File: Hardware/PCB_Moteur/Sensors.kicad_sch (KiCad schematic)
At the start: 18 parts, among them J18 Screw_Terminal_01x04, J3 Screw_Terminal_01x04, U8 INA125UA/2K5, U9 MAX6612MXK

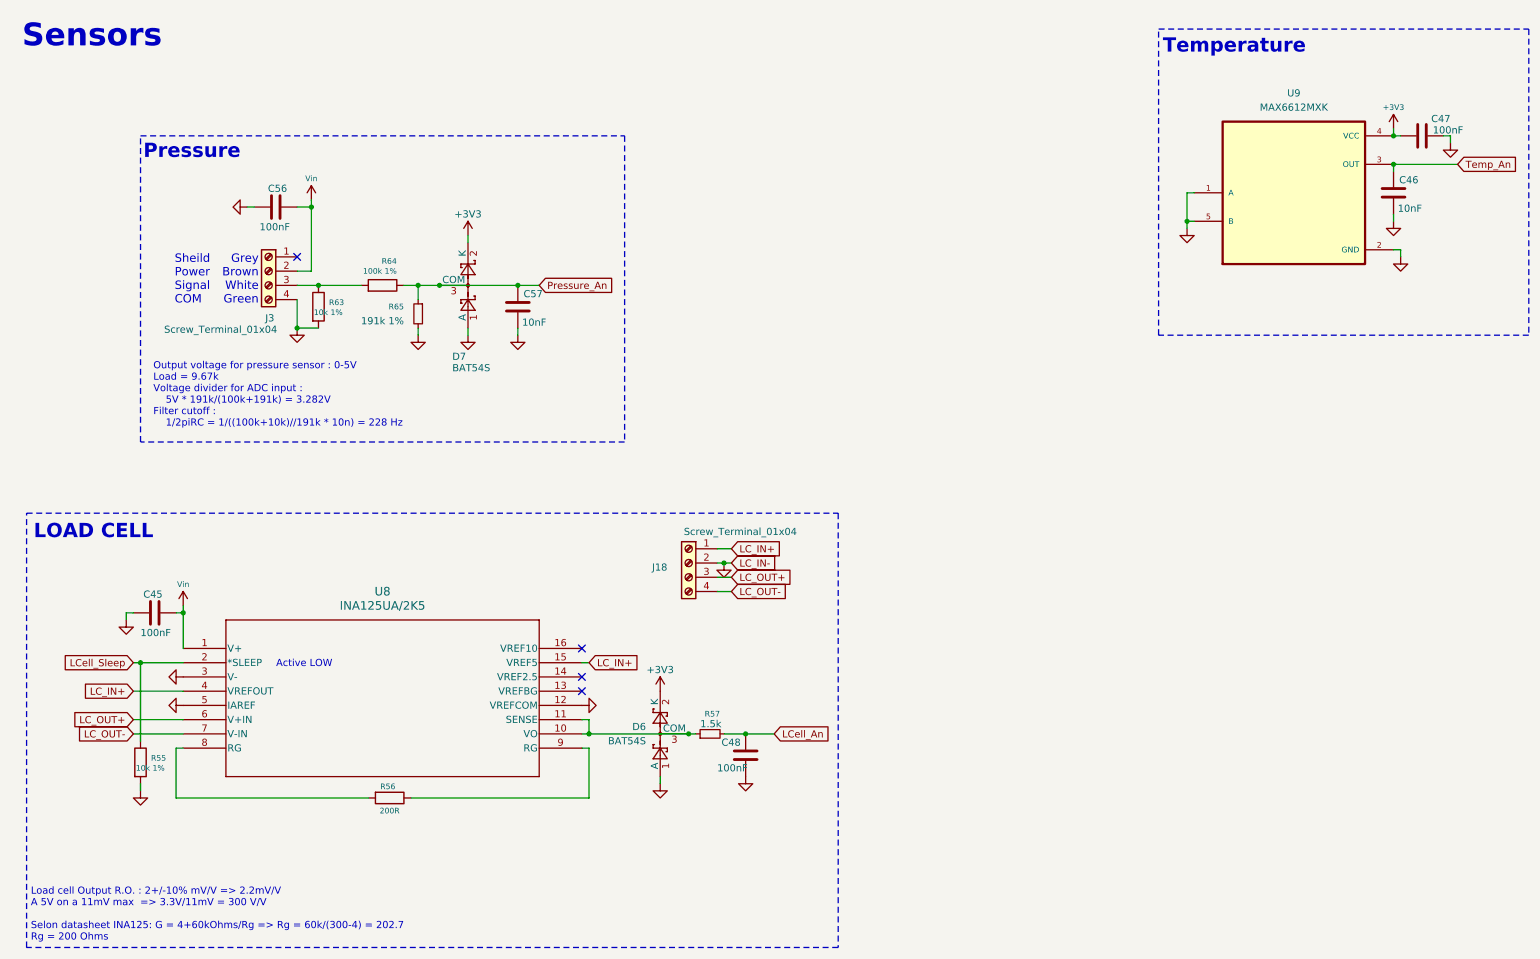
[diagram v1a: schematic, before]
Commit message: wip : reorder refdes and fix footprints
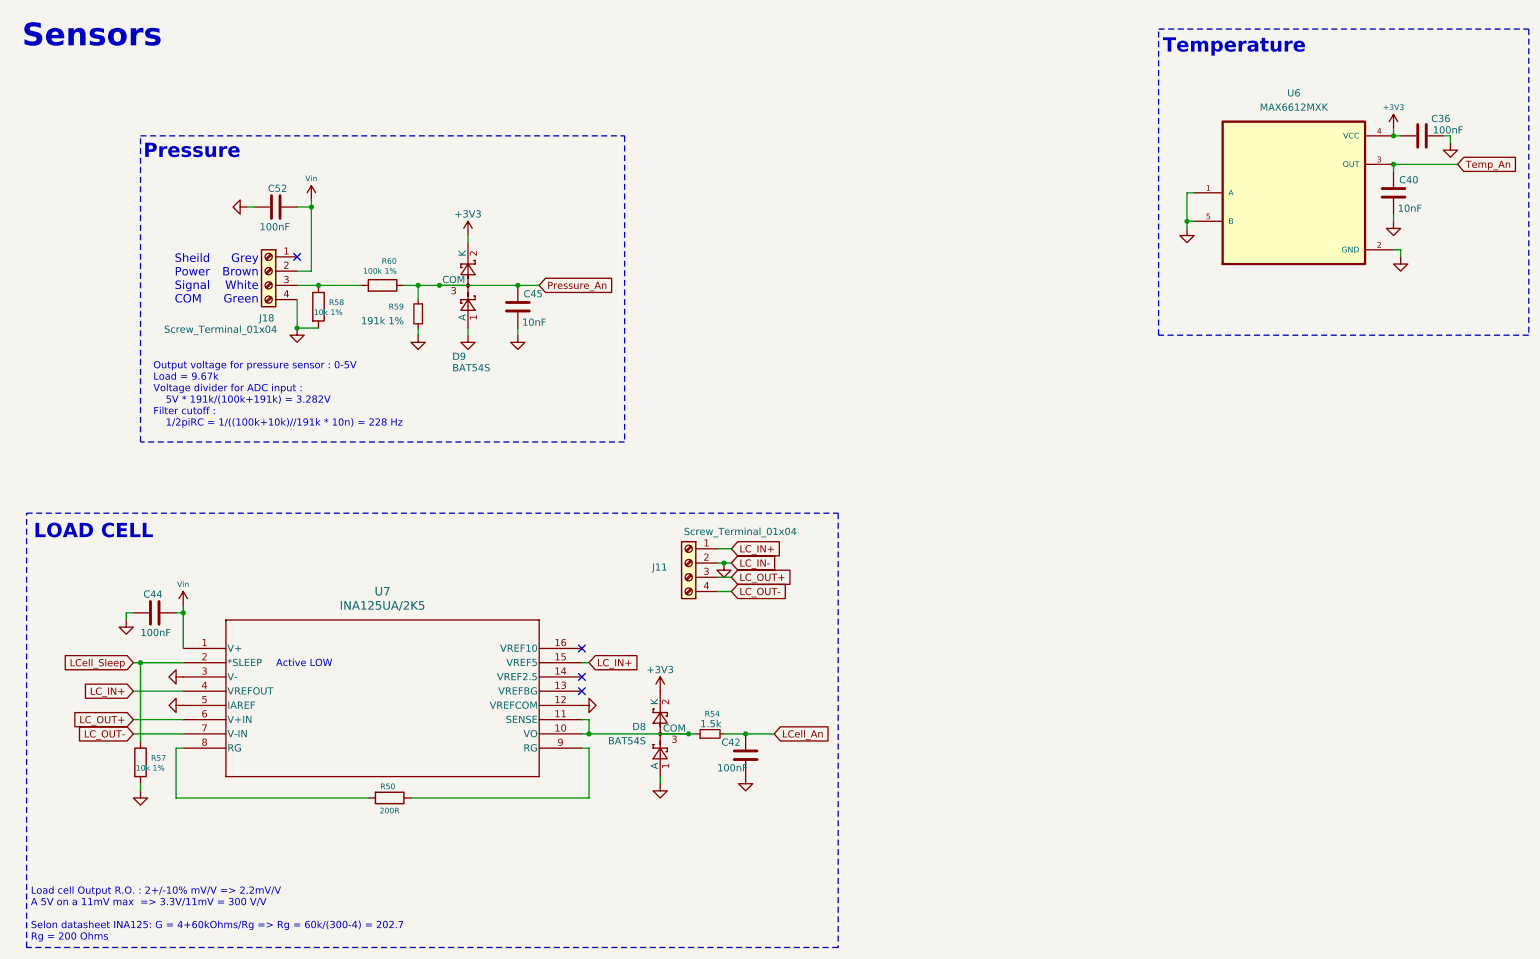
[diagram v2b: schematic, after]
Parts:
- U7: renamed from U8; DigiKey_Part_Number  (none) -> 296-50343-1-ND
- renumbered C47 to C36, C46 to C40, C48 to C42, C45 to C44, C57 to C45, C56 to C52, D6 to D8, D7 to D9, J18 to J11, J3 to J18, R56 to R50, R57 to R54, R55 to R57, R63 to R58, R65 to R59, R64 to R60, U9 to U6
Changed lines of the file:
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@@
 		(dnp no)
 		(fields_autoplaced yes)
-		(property "Reference" "D6"
+		(property "Reference" "D8"
 			(at 124.46 139.6999 90)
 			(effects
@@
 			(project "PCB_moteur"
 				(path "/b0d87684-7b1c-41d8-8358-755aa327573e/f31687d3-ca84-4d71-914a-32b6c2b363a9"
-					(reference "D6")
+					(reference "D8")
 					(unit 1)
 				)
@@
 		(on_board yes)
 		(dnp no)
-		(property "Reference" "R57"
+		(property "Reference" "R54"
 			(at 137.668 137.414 90)
 			(effects
@@
 			(project "PCB_moteur"
 				(path "/b0d87684-7b1c-41d8-8358-755aa327573e/f31687d3-ca84-4d71-914a-32b6c2b363a9"
-					(reference "R57")
+					(reference "R54")
 					(unit 1)
 				)
@@
 		(on_board yes)
 		(dnp no)
-		(property "Reference" "C47"
+		(property "Reference" "C36"
 			(at 267.97 31.242 90)
 			(effects
@@
 			(project "PCB_moteur"
 				(path "/b0d87684-7b1c-41d8-8358-755aa327573e/f31687d3-ca84-4d71-914a-32b6c2b363a9"
-					(reference "C47")
+					(reference "C36")
 					(unit 1)
 				)
@@
 		(on_board yes)
 		(dnp no)
-		(property "Reference" "C56"
+		(property "Reference" "C52"
 			(at 60.452 43.688 90)
 			(effects
@@
 			(project "PCB_moteur"
 				(path "/b0d87684-7b1c-41d8-8358-755aa327573e/f31687d3-ca84-4d71-914a-32b6c2b363a9"
-					(reference "C56")
+					(reference "C52")
 					(unit 1)
 				)
@@
 		(dnp no)
 		(fields_autoplaced yes)
-		(property "Reference" "U8"
+		(property "Reference" "U7"
 			(at 77.47 115.57 0)
 			(effects
@@
 			)
 		)
+		(property "DigiKey_Part_Number " "296-50343-1-ND"
+			(at 41.91 125.73 0)
+			(effects
+				(font
+					(size 1.27 1.27)
+				)
+				(hide yes)
+			)
+		)
 		(pin "4"
 		)
@@
 			(project "PCB_moteur"
 				(path "/b0d87684-7b1c-41d8-8358-755aa327573e/f31687d3-ca84-4d71-914a-32b6c2b363a9"
-					(reference "U8")
+					(reference "U7")
 					(unit 1)
 				)
@@
 		(on_board yes)
 		(dnp no)
-		(property "Reference" "C46"
+		(property "Reference" "C40"
 			(at 258.826 42.164 0)
 			(effects
@@
 			(project "PCB_moteur"
 				(path "/b0d87684-7b1c-41d8-8358-755aa327573e/f31687d3-ca84-4d71-914a-32b6c2b363a9"
-					(reference "C46")
+					(reference "C40")
 					(unit 1)
 				)
@@
 		(dnp no)
 		(fields_autoplaced yes)
-		(property "Reference" "U9"
+		(property "Reference" "U6"
 			(at 240.03 26.67 0)
 			(effects
@@
 			(project ""
 				(path "/b0d87684-7b1c-41d8-8358-755aa327573e/f31687d3-ca84-4d71-914a-32b6c2b363a9"
-					(reference "U9")
+					(reference "U6")
 					(unit 1)
 				)
@@
 		(on_board yes)
 		(dnp no)
-		(property "Reference" "J3"
+		(property "Reference" "J18"
 			(at 58.166 66.802 0)
 			(effects
@@
 			(project "PCB_moteur"
 				(path "/b0d87684-7b1c-41d8-8358-755aa327573e/f31687d3-ca84-4d71-914a-32b6c2b363a9"
-					(reference "J3")
+					(reference "J18")
 					(unit 1)
 				)
@@
 		(on_board yes)
 		(dnp no)
-		(property "Reference" "C48"
+		(property "Reference" "C42"
 			(at 137.922 142.494 0)
 			(effects
@@
 			(project "PCB_moteur"
 				(path "/b0d87684-7b1c-41d8-8358-755aa327573e/f31687d3-ca84-4d71-914a-32b6c2b363a9"
-					(reference "C48")
+					(reference "C42")
 					(unit 1)
 				)
@@
 		(on_board yes)
 		(dnp no)
-		(property "Reference" "D7"
+		(property "Reference" "D9"
 			(at 89.916 73.66 90)
 			(effects
@@
 			(project "PCB_moteur"
 				(path "/b0d87684-7b1c-41d8-8358-755aa327573e/f31687d3-ca84-4d71-914a-32b6c2b363a9"
-					(reference "D7")
+					(reference "D9")
 					(unit 1)
 				)
@@
 		(on_board yes)
 		(dnp no)
-		(property "Reference" "R56"
+		(property "Reference" "R50"
 			(at 79.756 150.368 90)
 			(effects
@@
 			(project "PCB_moteur"
 				(path "/b0d87684-7b1c-41d8-8358-755aa327573e/f31687d3-ca84-4d71-914a-32b6c2b363a9"
-					(reference "R56")
+					(reference "R50")
 					(unit 1)
 				)
@@
 		(on_board yes)
 		(dnp no)
-		(property "Reference" "R65"
+		(property "Reference" "R59"
 			(at 81.28 64.7699 0)
 			(effects
@@
 			(project "PCB_moteur"
 				(path "/b0d87684-7b1c-41d8-8358-755aa327573e/f31687d3-ca84-4d71-914a-32b6c2b363a9"
-					(reference "R65")
+					(reference "R59")
 					(unit 1)
 				)
@@
 		(on_board yes)
 		(dnp no)
-		(property "Reference" "C57"
+		(property "Reference" "C45"
 			(at 102.616 62.484 0)
 			(effects
@@
 			(project "PCB_moteur"
 				(path "/b0d87684-7b1c-41d8-8358-755aa327573e/f31687d3-ca84-4d71-914a-32b6c2b363a9"
-					(reference "C57")
+					(reference "C45")
 					(unit 1)
 				)
@@
 		(on_board yes)
 		(dnp no)
-		(property "Reference" "J18"
+		(property "Reference" "J11"
 			(at 128.27 111.252 0)
 			(effects
@@
 			(project "PCB_moteur"
 				(path "/b0d87684-7b1c-41d8-8358-755aa327573e/f31687d3-ca84-4d71-914a-32b6c2b363a9"
-					(reference "J18")
+					(reference "J11")
 					(unit 1)
 				)
@@
 		(on_board yes)
 		(dnp no)
-		(property "Reference" "R55"
+		(property "Reference" "R57"
 			(at 38.862 145.288 0)
 			(effects
@@
 			(project "PCB_moteur"
 				(path "/b0d87684-7b1c-41d8-8358-755aa327573e/f31687d3-ca84-4d71-914a-32b6c2b363a9"
-					(reference "R55")
+					(reference "R57")
 					(unit 1)
 				)
@@
 		(on_board yes)
 		(dnp no)
-		(property "Reference" "R64"
+		(property "Reference" "R60"
 			(at 80.01 56.642 90)
 			(effects
@@
 			(project "PCB_moteur"
 				(path "/b0d87684-7b1c-41d8-8358-755aa327573e/f31687d3-ca84-4d71-914a-32b6c2b363a9"
-					(reference "R64")
+					(reference "R60")
 					(unit 1)
 				)
@@
 		(on_board yes)
 		(dnp no)
-		(property "Reference" "R63"
+		(property "Reference" "R58"
 			(at 70.612 64.008 0)
 			(effects
@@
 			(project "PCB_moteur"
 				(path "/b0d87684-7b1c-41d8-8358-755aa327573e/f31687d3-ca84-4d71-914a-32b6c2b363a9"
-					(reference "R63")
+					(reference "R58")
 					(unit 1)
 				)
@@
 		(on_board yes)
 		(dnp no)
-		(property "Reference" "C45"
+		(property "Reference" "C44"
 			(at 34.798 116.078 90)
 			(effects
@@
 			(project "PCB_moteur"
 				(path "/b0d87684-7b1c-41d8-8358-755aa327573e/f31687d3-ca84-4d71-914a-32b6c2b363a9"
-					(reference "C45")
+					(reference "C44")
 					(unit 1)
 				)

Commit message: fix(moteur + gse): gnd not connected for pressure sensor + seperate alim pressure sensor for motor pcb
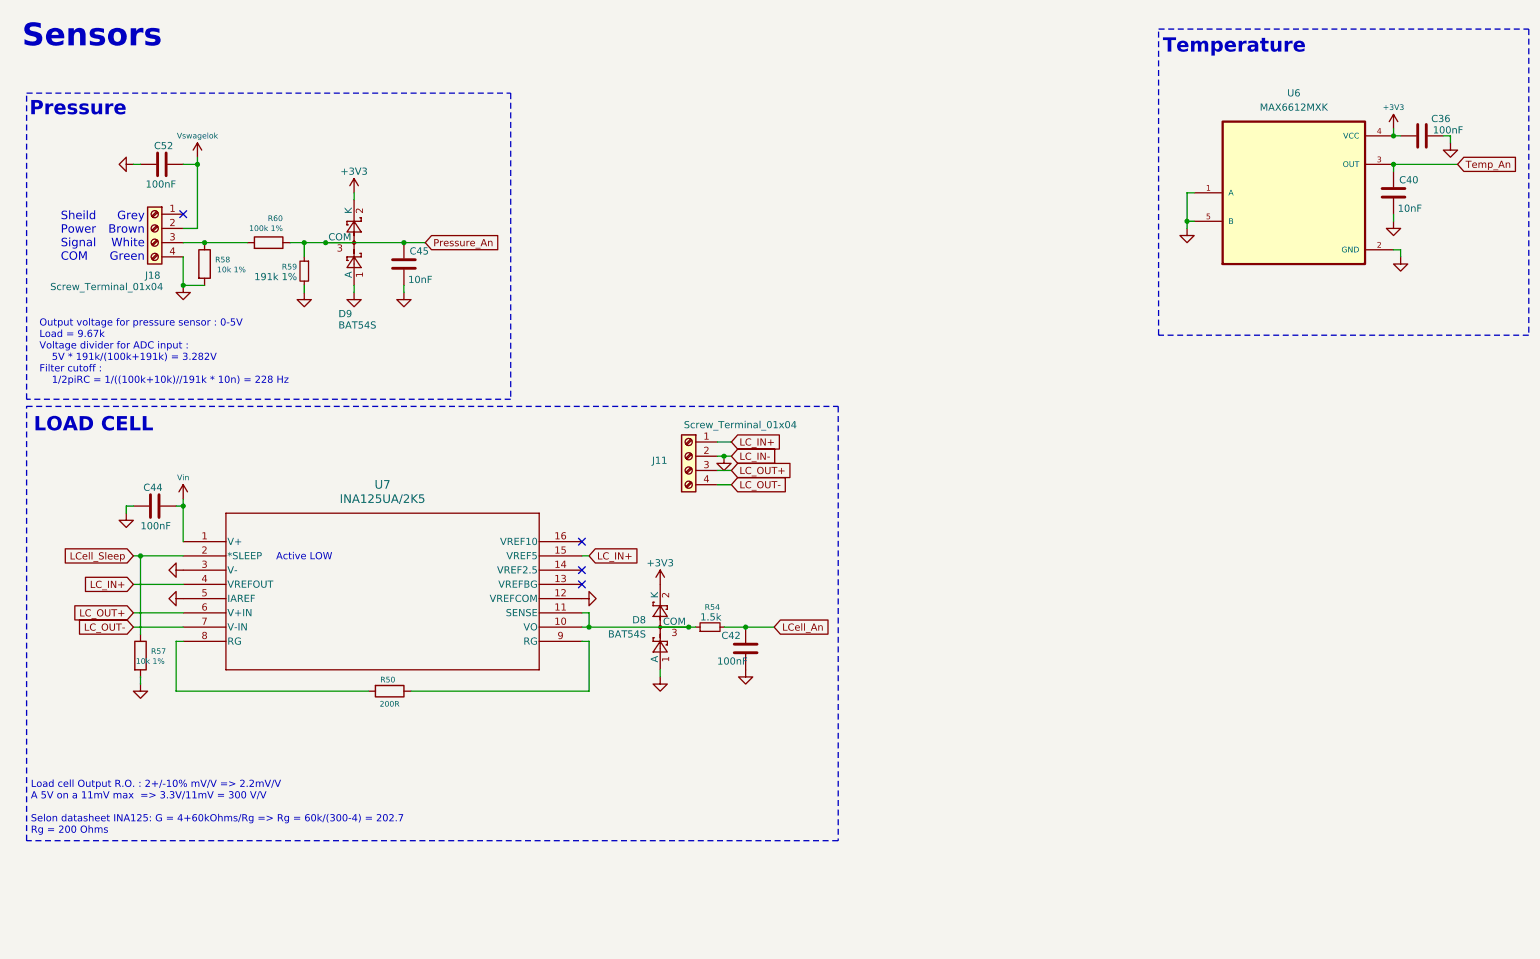
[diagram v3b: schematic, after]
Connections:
- net Vin: no longer C52.2, J18.2 (Pin_2)
- new net Vswagelok: C52.2, J18.2 (Pin_2)
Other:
- moved on the sheet: C42, C44, C45, C52, D8, D9, J11, J18, R50, R54, R57, R58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

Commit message: fix(moteur + gse): move xt30 to border + fix silkscreen + connect shield to gnd  in pressure sensor + remake rounded corners + fix/add doc
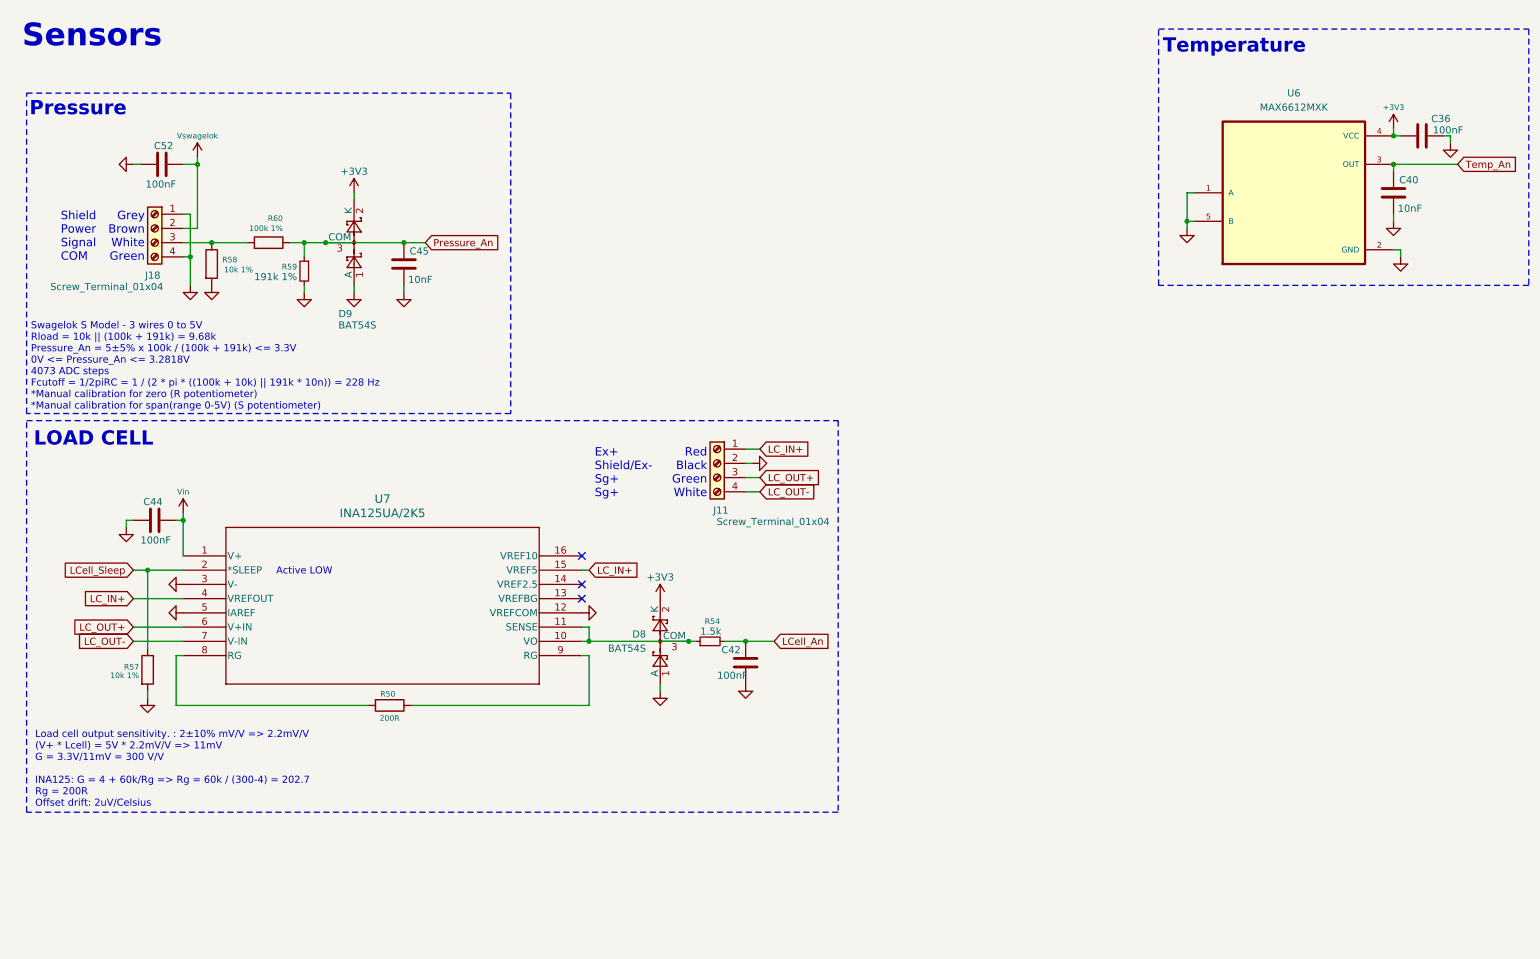
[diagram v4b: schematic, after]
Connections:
- net GND: now also J18.1 (Pin_1)
- no-connect marks 4 -> 3
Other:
- note added: "Ex+ Shield/Ex- Sg+ Sg+"
- note added: "Load cell output sensitivity. : 2±10% mV/V => 2.2mV/V (V+ * Lcell) = 5V * 2.2mV/V => 11mV G = 3.3V/11mV = 300 V/V INA125: G = 4 + 60k/Rg => Rg = 60k / (300-4) = 202.7 Rg = 200R Offset drift: 2uV/Celsius"
- note added: "Red Black Green White"
- note added: "Shield Power Signal COM"
- note added: "Swagelok S Model - 3 wires 0 to 5V Rload = 10k || (100k + 191k) = 9.68k Pressure_An = 5±5% x 100k / (100k + 191k) <= 3.3V 0V <= Pressure_An <= 3.2818V 4073 ADC steps Fcutoff = 1/2piRC = 1 / (2 * pi * ((100k + 10k) || 191k * 10n)) = 228 Hz *Manual calibration for zero (R potentiometer) *Manual calibration for span(range 0-5V) (S potentiometer)"
- note removed: "Load cell Output R.O. : 2+/-10% mV/V => 2.2mV/V A 5V on a 11mV max => 3.3V/11mV = 300 V/V Selon datasheet INA125: G = 4+60kOhms/Rg => Rg = 60k/(300-4) = 202.7 Rg = 200 Ohms"
- note removed: "Output voltage for pressure sensor : 0-5V Load = 9.67k Voltage divider for ADC input : 5V * 191k/(100k+191k) = 3.282V Filter cutoff : 1/2piRC = 1/((100k+10k)//191k * 10n) = 228 Hz"
- note removed: "Sheild Power Signal COM"
- moved on the sheet: C42, C44, D8, J11, R50, R54, R57, R58, U7
